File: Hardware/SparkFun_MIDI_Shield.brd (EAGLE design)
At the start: 59.7 x 53.3 mm, 32 parts, among them J1 MIDI IN, J2 MIDI OUT, J3 UNO_R3_SHIELD, U2 74AHC1G125

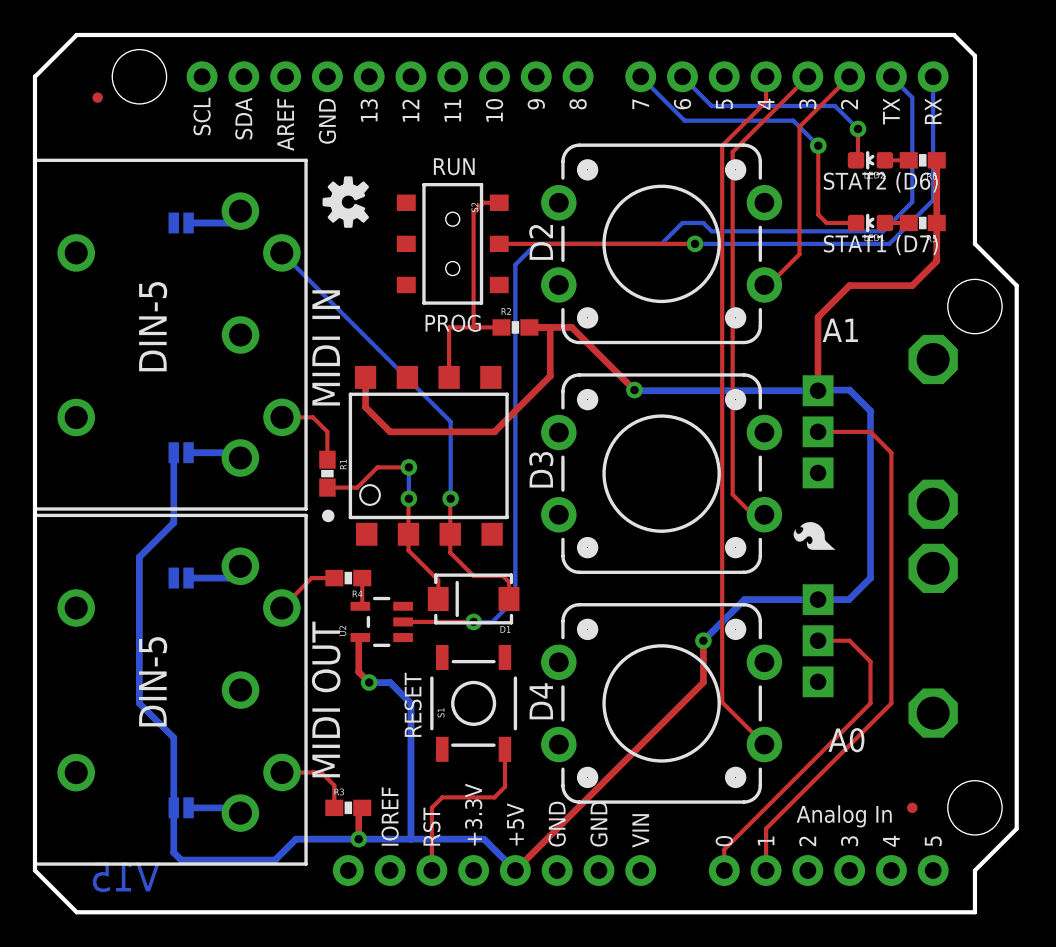
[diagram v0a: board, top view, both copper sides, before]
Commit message: Updates after engineering review.
Added jumper to allow optional soft serial.
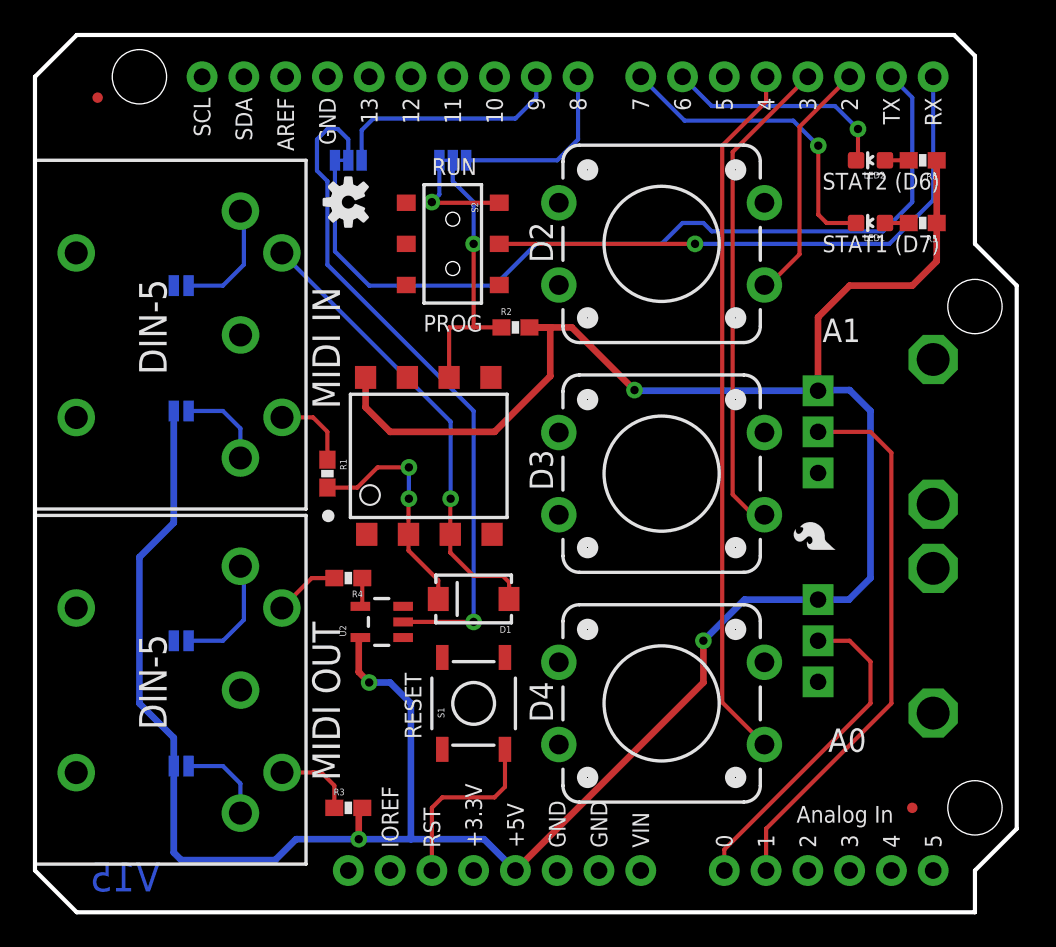
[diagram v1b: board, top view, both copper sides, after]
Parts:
- added SJ1: TX sel, SparkFun-Passives:PAD-JUMPER-3-2OF3_NC_BY_TRACE_YES_SILK_FULL_BOX
- added SJ2: RX sel, SparkFun-Passives:PAD-JUMPER-3-2OF3_NC_BY_TRACE_YES_SILK_FULL_BOX
- moved JP3 3.81 mm to (8.89, 16.5)
- moved JP1 3.81 mm to (8.89, 38.1)
- moved JP4 2.54 mm to (8.89, 8.89)
- moved JP2 2.54 mm to (8.89, 30.5)
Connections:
- removed net RX: R2.1, S2.1, U$1.6
- removed net TX: J3.TX, U2.2
- new net HARD-RX: S2.1, SJ1.3
- new net HARD-TX: J3.TX, SJ2.3
- new net PORT-RX: R2.1, SJ1.2, U$1.6
- new net PORT-TX: SJ2.2, U2.2
- new net SOFT-RX: J3.D8, SJ1.1
- new net SOFT-TX: J3.D9, SJ2.1
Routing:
- net TX: track 62.0 -> 0.00 mm, vias 1 -> 0
- net HARD-TX: track 0.00 -> 52.2 mm
- net PORT-TX: track 0.00 -> 41.3 mm, vias 0 -> 1
- net PORT-RX: track 0.00 -> 16.9 mm, vias 0 -> 1
- net RX: track 15.0 -> 0.00 mm
- net SOFT-TX: track 0.00 -> 14.5 mm
- net SOFT-RX: track 0.00 -> 11.1 mm
- net HARD-RX: track 0.00 -> 6.84 mm, vias 0 -> 1
- net N$6: track 3.45 -> 7.23 mm
- net N$4: track 3.45 -> 7.23 mm
- net VCC: track 168.5 -> 171.1 mm
- net N$5: track 3.28 -> 5.39 mm
- net N$7: track 3.28 -> 5.39 mm
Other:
- board text added: "Hardware (0,1)"
- board text added: "JP1&2 Power On MIDI Input"
- board text added: "JP3&4 Power On MIDI Output"
- board text added: "SJ1"
- board text added: "SJ1&2 select UART"
- board text added: "SJ2"
- board text added: "Software (8,9)"

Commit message: Updates after QC checklist.
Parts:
- renumbered U$1 to U1
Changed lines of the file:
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@@
 <layer number="18" name="Vias" color="2" fill="1" visible="yes" active="yes"/>
 <layer number="19" name="Unrouted" color="6" fill="1" visible="yes" active="yes"/>
-<layer number="20" name="Dimension" color="15" fill="1" visible="yes" active="yes"/>
+<layer number="20" name="Dimension" color="15" fill="1" visible="no" active="yes"/>
 <layer number="21" name="tPlace" color="16" fill="1" visible="yes" active="yes"/>
-<layer number="22" name="bPlace" color="14" fill="1" visible="yes" active="yes"/>
+<layer number="22" name="bPlace" color="14" fill="1" visible="no" active="yes"/>
 <layer number="23" name="tOrigins" color="15" fill="1" visible="yes" active="yes"/>
-<layer number="24" name="bOrigins" color="15" fill="1" visible="yes" active="yes"/>
+<layer number="24" name="bOrigins" color="15" fill="1" visible="no" active="yes"/>
 <layer number="25" name="tNames" color="7" fill="1" visible="no" active="yes"/>
 <layer number="26" name="bNames" color="7" fill="1" visible="no" active="yes"/>
@@
 <attribute name="PROD_ID" value="SWCH-08179" x="25.4" y="40.64" size="1.778" layer="27" font="vector" ratio="15" rot="R270" display="off"/>
 </element>
-<element name="U$1" library="SparkFun-DiscreteSemi" package="8-SMD" value="6N138M" x="24.13" y="27.94">
-<attribute name="PROD_ID" value="IC-09482" x="24.13" y="27.94" size="1.778" layer="27" font="vector" ratio="15" display="off"/>
-</element>
 <element name="JP3" library="SparkFun-Passives" package="PAD-JUMPER-2-NO_YES_SILK" value="JUMPER-PAD-2-NOYES_SILK" x="8.89" y="16.51" rot="MR180"/>
 <element name="JP4" library="SparkFun-Passives" package="PAD-JUMPER-2-NO_YES_SILK" value="JUMPER-PAD-2-NOYES_SILK" x="8.89" y="8.89" rot="MR180"/>
@@
 <element name="SJ1" library="SparkFun-Passives" package="PAD-JUMPER-3-2OF3_NC_BY_TRACE_YES_SILK_FULL_BOX" value="TX sel" x="25.4" y="45.72" rot="MR0"/>
 <element name="SJ2" library="SparkFun-Passives" package="PAD-JUMPER-3-2OF3_NC_BY_TRACE_YES_SILK_FULL_BOX" value="RX sel" x="19.05" y="45.72" rot="MR0"/>
+<element name="U1" library="SparkFun-DiscreteSemi" package="8-SMD" value="6N138M" x="24.13" y="27.94">
+<attribute name="PROD_ID" value="IC-09482" x="24.13" y="27.94" size="1.778" layer="27" font="vector" ratio="15" display="off"/>
+</element>
 </elements>
 <signals>
@@
 <contactref element="U2" pad="1"/>
 <contactref element="S1" pad="1"/>
-<contactref element="U$1" pad="5"/>
 <contactref element="JP3" pad="1"/>
 <contactref element="JP1" pad="1"/>
+<contactref element="U1" pad="5"/>
 </signal>
 <signal name="VCC">
@@
 <wire x1="30.06" y1="35.56" x2="32.639" y2="35.56" width="0.4064" layer="1"/>
 <wire x1="32.639" y1="35.56" x2="36.449" y2="31.75" width="0.4064" layer="1"/>
-<contactref element="U$1" pad="8"/>
-<wire x1="20.1" y1="32.52" x2="20.1" y2="30.7" width="0.4064" layer="1"/>
 <wire x1="20.1" y1="30.7" x2="21.59" y2="29.21" width="0.4064" layer="1"/>
 <wire x1="21.59" y1="29.21" x2="27.94" y2="29.21" width="0.4064" layer="1"/>
@@
 <wire x1="19.685" y1="16.6061" x2="19.685" y2="14.605" width="0.4064" layer="1"/>
 <wire x1="19.685" y1="14.605" x2="20.32" y2="13.97" width="0.4064" layer="1"/>
+<contactref element="U1" pad="8"/>
+<wire x1="20.1" y1="32.52" x2="20.1" y2="30.7" width="0.4064" layer="1"/>
 </signal>
 <signal name="56">
@@
 <wire x1="22.71" y1="21.994" x2="24.52" y2="20.184" width="0.254" layer="1"/>
 <wire x1="17.78" y1="25.82" x2="19.597" y2="25.82" width="0.254" layer="1"/>
-<contactref element="U$1" pad="2"/>
+<contactref element="U1" pad="2"/>
 <wire x1="22.71" y1="22.98" x2="22.71" y2="21.994" width="0.254" layer="1"/>
 <wire x1="22.71" y1="22.98" x2="22.71" y2="25.123" width="0.254" layer="1"/>
@@
 <wire x1="28.829" y1="19.059" x2="28.82" y2="19.05" width="0.254" layer="1"/>
 <wire x1="25.273" y1="29.827" x2="15.01" y2="40.09" width="0.254" layer="16"/>
-<contactref element="U$1" pad="3"/>
+<contactref element="U1" pad="3"/>
+<wire x1="25.25" y1="22.98" x2="25.25" y2="21.867" width="0.254" layer="1"/>
 <wire x1="25.25" y1="22.98" x2="25.25" y2="25.123" width="0.254" layer="1"/>
 <wire x1="25.25" y1="25.123" x2="25.273" y2="25.146" width="0.254" layer="1"/>
-<wire x1="25.25" y1="22.98" x2="25.25" y2="21.867" width="0.254" layer="1"/>
 </signal>
 <signal name="PORT-RX">
 <contactref element="R2" pad="1"/>
-<contactref element="U$1" pad="6"/>
-<wire x1="25.18" y1="32.52" x2="25.18" y2="35.56" width="0.254" layer="1"/>
 <wire x1="28.36" y1="35.56" x2="26.67" y2="35.56" width="0.254" layer="1"/>
 <contactref element="SJ1" pad="2"/>
@@
 <wire x1="26.67" y1="43.18" x2="26.67" y2="40.64" width="0.254" layer="16"/>
 <wire x1="26.67" y1="40.64" x2="26.67" y2="35.56" width="0.254" layer="1"/>
-<wire x1="26.67" y1="35.56" x2="25.18" y2="35.56" width="0.254" layer="1"/>
 <via x="26.67" y="40.64" extent="1-16" drill="0.508"/>
+<wire x1="25.18" y1="35.086" x2="25.654" y2="35.56" width="0.254" layer="1"/>
+<wire x1="25.654" y1="35.56" x2="26.67" y2="35.56" width="0.254" layer="1"/>
+<contactref element="U1" pad="6"/>
+<wire x1="25.18" y1="32.52" x2="25.18" y2="35.086" width="0.254" layer="1"/>
 </signal>
 <signal name="1235">

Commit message: Prototype Revisions WIP
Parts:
- J1, J2: device Testing:5-PIN-DIN-RA-PCB -> Testing:5-PIN-DIN-RA-PCB-NEW
- J3: device Testing:UNO_R3_SHIELD_HOLES -> SparkFun-Boards:UNO_R3_SHIELD
- moved LOGO2 14.2 mm to (6.35, 49.5)
- moved J1 8.98 mm to (0.00, 34.3)
- moved J2 8.89 mm to (0.00, 14.0)
- moved RV2 2.54 mm to (54.6, 14.0)
- moved RV1 2.54 mm to (54.6, 31.8)
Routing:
- net A1: track 33.5 -> 36.1 mm
- net A0: track 20.1 -> 18.3 mm
- net N$6: track 7.23 -> 6.02 mm
- net VCC: track 171.1 -> 172.0 mm
- net PIN5: track 27.8 -> 27.0 mm
- net N$5: track 5.39 -> 4.75 mm
- net N$7: track 5.39 -> 6.02 mm
- net N$2: track 4.81 -> 4.21 mm

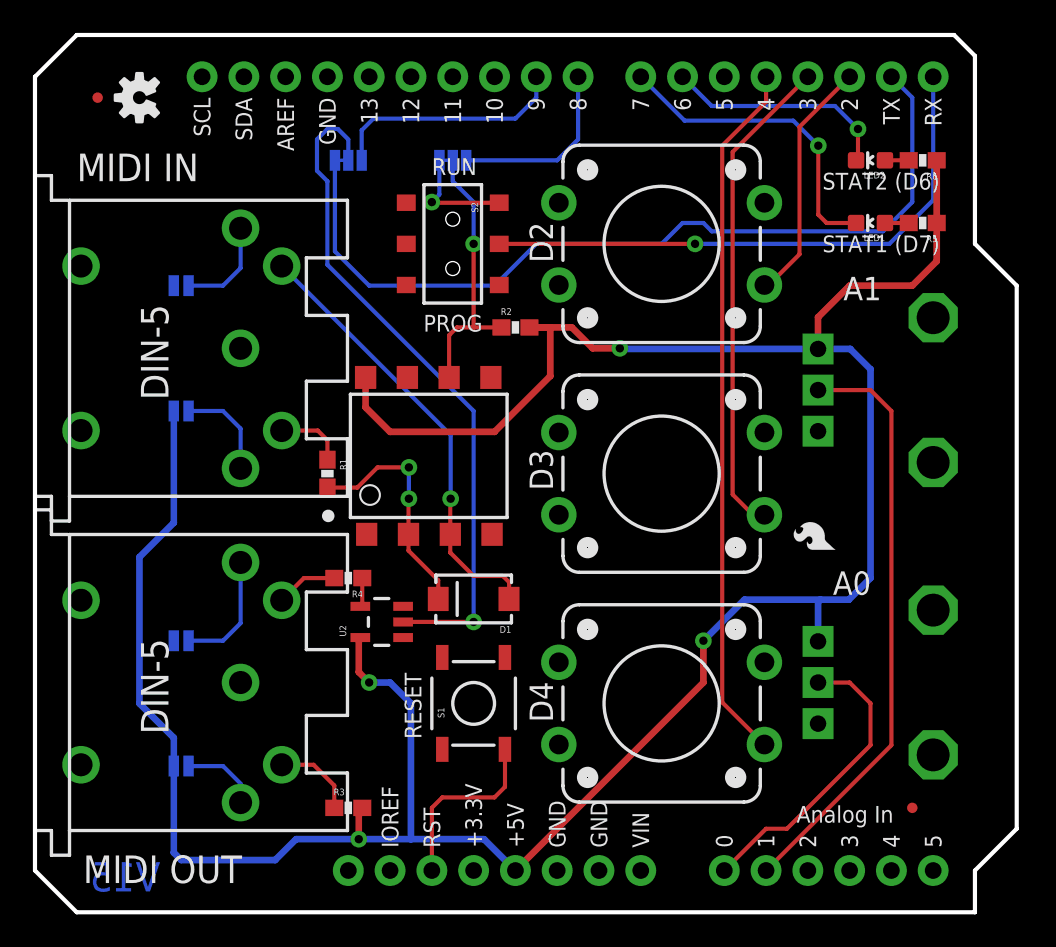
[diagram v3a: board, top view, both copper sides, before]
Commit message: WIP Mostly complete.
Proto issues handles.
-Pots turn the right way.
-Option for out vs thru.
-JP/SJ terminology resolved.
-More clearance around new connector component.
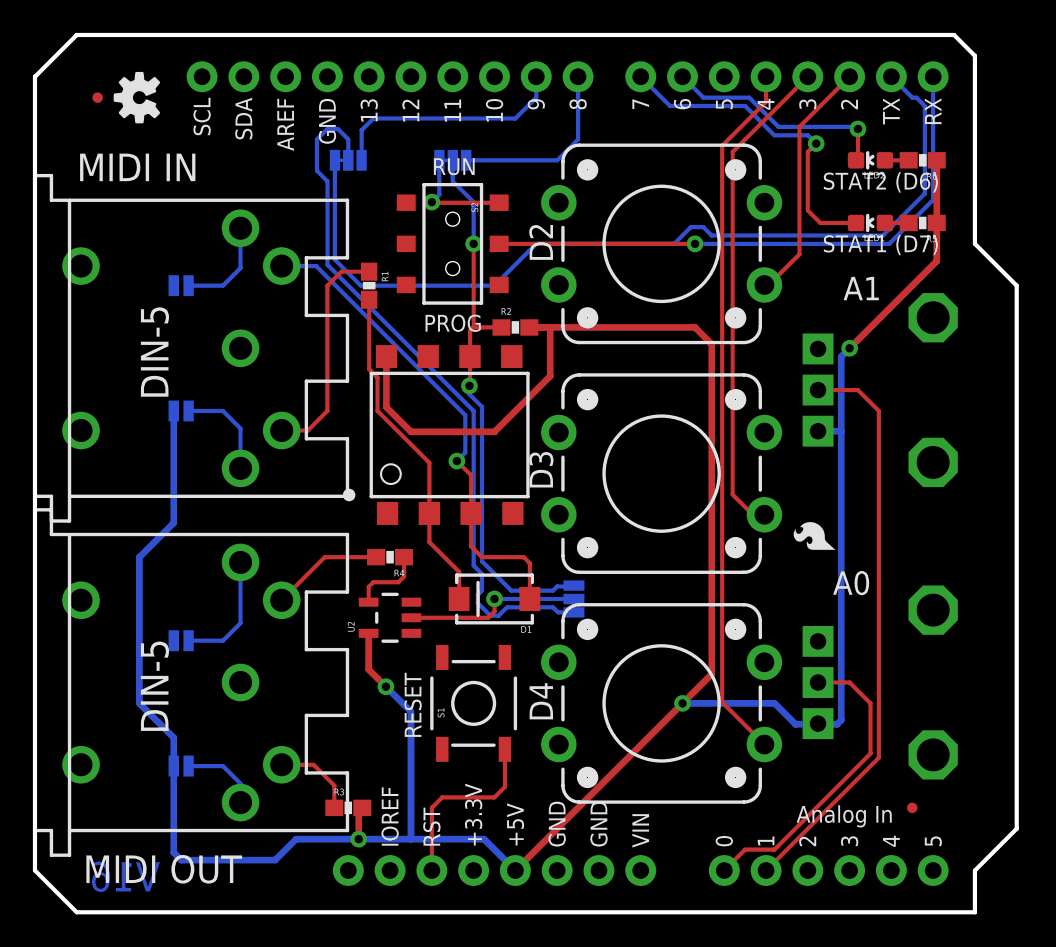
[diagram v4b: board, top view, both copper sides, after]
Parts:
- added SJ3: out/thru, SparkFun-Passives:PAD-JUMPER-3-2OF3_NC_BY_TRACE_YES_SILK_FULL_BOX
- moved R1 11.7 mm to (20.3, 38.1)
- moved R4 2.84 mm to (21.6, 21.6)
- moved U1 1.80 mm to (25.4, 29.2)
- moved D1 1.27 mm to (27.9, 19.1)
- moved U2 0.57 mm to (21.6, 17.9)
- renumbered JP1 to SJ4, JP2 to SJ5, JP3 to SJ6, JP4 to SJ7
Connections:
- new net TX-BUF: SJ3.2, U2.2
- net GND: now also RV1.P$1, RV2.P$1; no longer RV1.P$3, RV2.P$3
- net PORT-RX: now also SJ3.1
- net PORT-TX: now also SJ3.3; no longer U2.2
- net VCC: now also RV1.P$3, RV2.P$3; no longer RV1.P$1, RV2.P$1
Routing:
- net PORT-RX: track 16.6 -> 33.5 mm, vias 1 -> 2
- net VCC: track 172.0 -> 183.6 mm
- net TX-BUF: track 0.00 -> 10.8 mm, vias 0 -> 1
- net N$2: track 4.21 -> 13.8 mm
- net 56: track 14.2 -> 20.5 mm, vias 2 -> 0
- net N$1: track 3.76 -> 6.83 mm
- net N$3: track 1.88 -> 4.52 mm
- net PIN5: track 27.0 -> 29.6 mm
- net PORT-TX: track 41.3 -> 42.7 mm, vias 1 -> 0
- net HARD-TX: track 52.2 -> 53.4 mm
- net A1: track 36.1 -> 35.0 mm
- net D7: track 19.2 -> 19.9 mm
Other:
- board text added: "MIDI Out"
- board text added: "MIDI Thru"
- board text added: "SJ3"
- board text added: "SJ3 selects out type"
- board text added: "SJ4"
- board text added: "SJ4 & 5 Power To MIDI Input"
- board text added: "SJ5"
- board text added: "SJ6"
- board text added: "SJ6 & 7 Power To MIDI Output"
- board text added: "SJ7"
- board text added: "V16"
- board text removed: "JP1"
- board text removed: "JP1&2 Power On MIDI Input"
- board text removed: "JP2"
- board text removed: "JP3"
- board text removed: "JP3&4 Power On MIDI Output"
- board text removed: "JP4"
- board text removed: "V15"

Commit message: Board updates.
Small tweaks before submission for review.
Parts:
- added U$1: REVISION, SparkFun-Aesthetics:REVISION
- moved LOGO2 57.0 mm to (56.9, 23.1)
- moved LOGO5 2.84 mm to (51.8, 22.2)
- moved R2 0.25 mm to (29.2, 35.8)
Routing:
- net SOFT-TX: track 14.5 -> 19.0 mm
- net VCC: track 183.6 -> 181.7 mm
- net PORT-TX: track 42.7 -> 41.9 mm
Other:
- board text added: "Chris Taylor"
